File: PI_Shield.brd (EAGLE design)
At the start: 72.4 x 72.4 mm, 74 parts, among them J10 T2I, J11 T2I, J12 T2I, J13 DF13-4P-1.25DSA, J14 DF13-4P-1.25DSA, J15 DF13-4P-1.25DSA, J16 T2I5P, Q1 220mA/50V/3.5Ω, Q2 220mA/50V/3.5Ω, Q3 220mA/50V/3.5Ω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

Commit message: General routing complete
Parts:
- moved C3 4.40 mm to (33.4, 45.6), flipped to the top
- moved R8 1.66 mm to (45.3, 25.0), turned to 180 degrees
- moved J4 1.02 mm to (34.0, 58.9)
- moved R6 1.02 mm to (37.1, 63.1)
- moved C11 0.68 mm to (30.0, 34.3)
- moved R7 0.64 mm to (37.1, 65.2)
- moved J11 0.63 mm to (40.0, 58.2)
- moved J10 0.46 mm to (40.0, 65.8)
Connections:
- removed net 3VO: U$4.3VO, U$5.3VO
- removed net DI: U$8.31
- removed net DI3: U$8.40
- new net 3VO_1: U$4.3VO
- new net 3VO_2: U$5.3VO
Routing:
- net SDA: track 0.02 -> 123.6 mm, vias 0 -> 7
- net SCL: track 0.02 -> 119.0 mm, vias 0 -> 6
- net CAN_P: track 0.00 -> 45.7 mm, vias 0 -> 1
- net CAN_N: track 0.00 -> 45.3 mm, vias 0 -> 1
- net RXCAN: track 0.00 -> 16.0 mm, vias 0 -> 1
- net TXCAN: track 0.00 -> 15.8 mm, vias 0 -> 1
- net INT: track 0.00 -> 15.8 mm
- net CLK: track 14.8 -> 30.4 mm
- net MOSI: track 20.2 -> 33.7 mm
- net TX: track 0.00 -> 12.8 mm
- net RX0_INT: track 0.00 -> 12.7 mm
- net RX: track 0.00 -> 12.7 mm
- net MISO: track 18.3 -> 28.9 mm
- net DI2: track 0.00 -> 10.4 mm
- net DI1: track 0.00 -> 10.1 mm
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
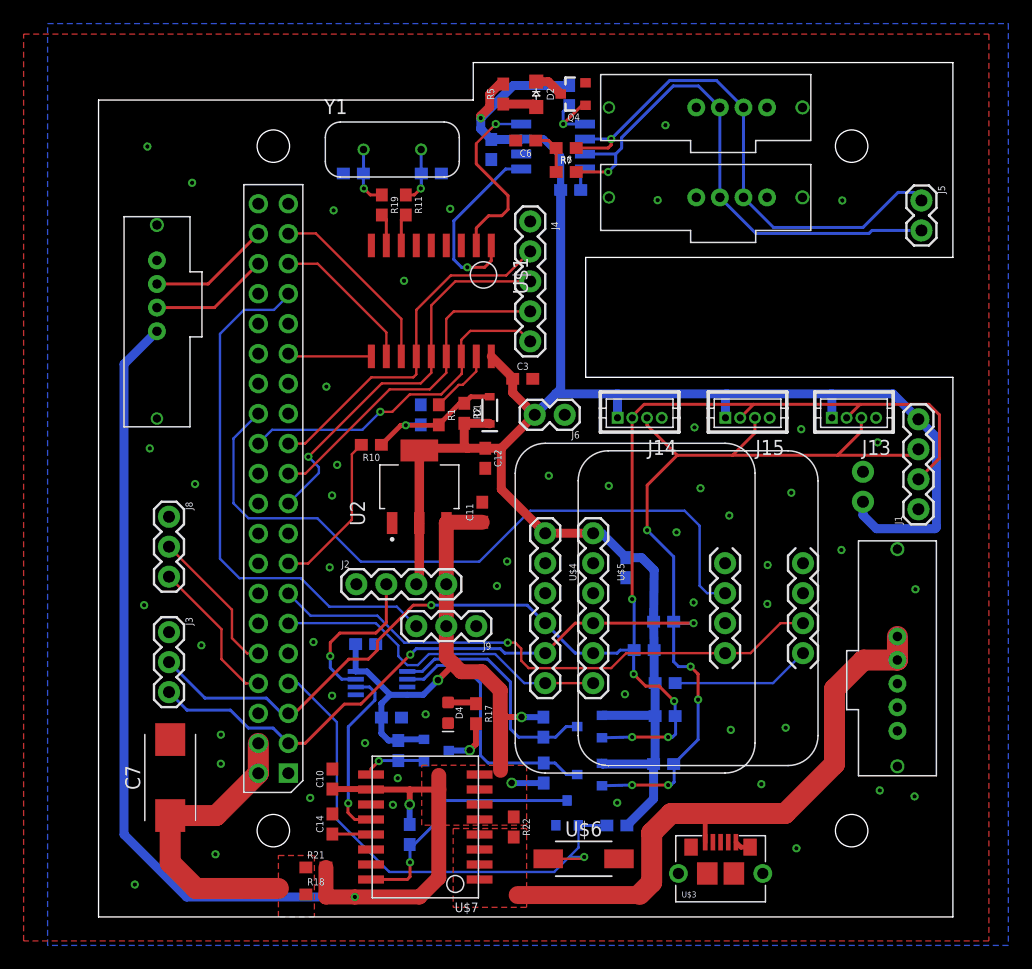
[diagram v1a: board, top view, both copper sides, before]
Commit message: Working on Impedance Matching
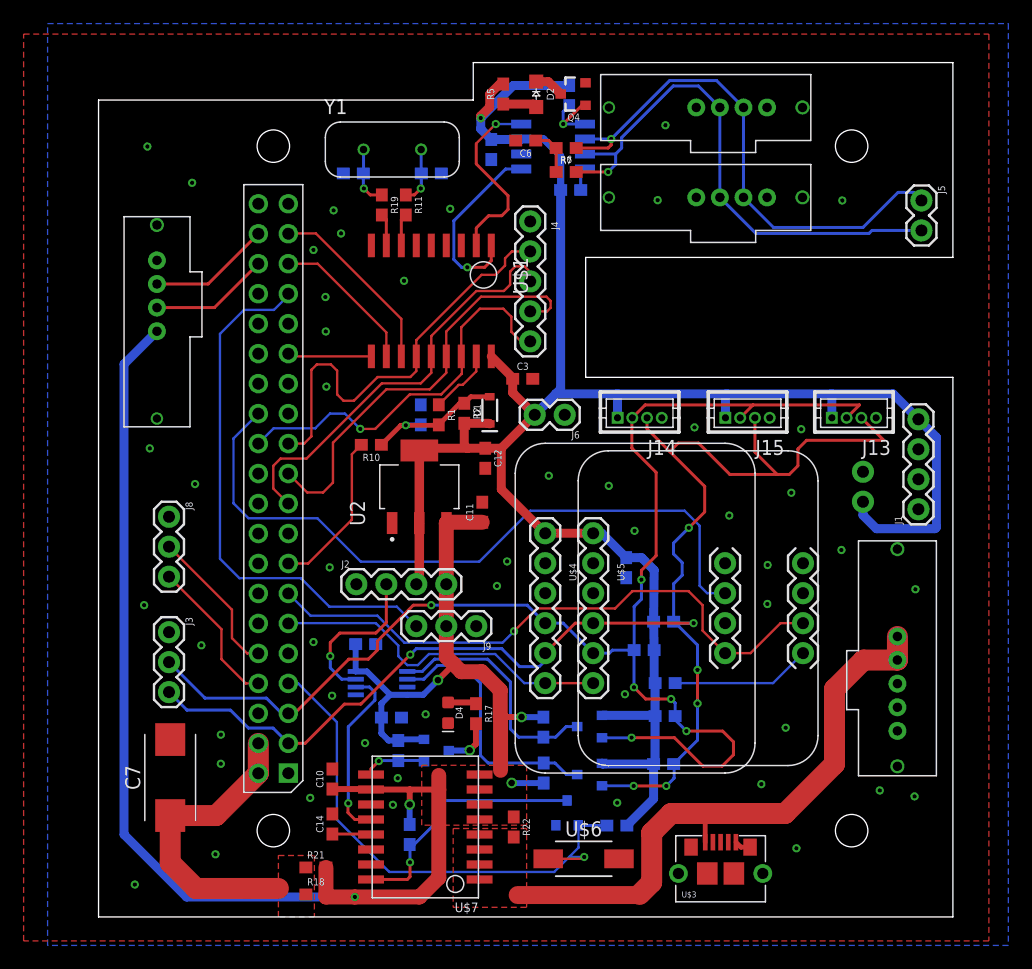
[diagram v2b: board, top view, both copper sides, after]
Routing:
- net MISO: track 28.9 -> 36.4 mm
- net CLK: track 30.4 -> 36.2 mm
- net CS: track 29.1 -> 33.1 mm
- net IMU_INT: track 48.4 -> 51.6 mm
- net SDA: track 123.6 -> 126.2 mm
- net MOSI: track 33.7 -> 36.0 mm, vias 1 -> 0
- net GND: vias 51 -> 49

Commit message: labels, routing touch ups, etc
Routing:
- net GND: track 1.37 -> 30.0 mm, vias 49 -> 65
- net SDA: track 126.2 -> 123.3 mm
- net SCL: track 119.4 -> 117.6 mm
- net 5V: track 152.5 -> 151.0 mm
- net OCD: track 9.96 -> 10.6 mm
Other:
- board size 72.4 x 72.4 mm -> 71.5 x 72.4 mm
- board text added: "5V - DI1 - DI2 - GND"
- board text added: "CAN_H - CAN_L"
- board text added: "CS - MISO - MOSI - CLK - GND"
- board text added: "GND - GND - NC - 5V - 5V"
- board text added: "GND - SCL - SDA - 3.3V"
- board text added: "PWM - 5V - GND"
- board text added: "SDA - SCL - GND"

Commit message: Finishing touches
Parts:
- added D3, D5: (no value), SparkFun-LED:LED-0603
- added R26, R27: (no value), SparkFun-Resistors:0603
- moved J12 7.79 mm to (6.25, 49.3)
- moved R17 3.18 mm to (26.3, 17.0), flipped to the bottom, turned to 180 degrees
- moved D4 2.65 mm to (29.5, 16.2)
- moved C8 1.86 mm to (20.4, 16.8), turned to 0 degrees
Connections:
- net CAN_N renamed CAN_L
- net CAN_P renamed CAN_H
- new net N$12: D5.A, R27.1
- new net N$9: D3.A, R26.1
- net 3V3: now also R27.2
- net 5V: now also R26.2
- net GND: now also D3.C, D5.C
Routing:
- net 3V3: track 183.8 -> 214.1 mm, vias 1 -> 2
- net SCL: track 117.6 -> 130.2 mm
- net 5V: track 151.0 -> 162.0 mm
- net SDA: track 123.3 -> 128.1 mm, vias 7 -> 8
- net GND: track 30.0 -> 33.9 mm, vias 65 -> 78
- net N$11: track 2.40 -> 6.29 mm, vias 0 -> 1
- net N$12: track 0.00 -> 3.85 mm
- net N$9: track 0.00 -> 3.06 mm, vias 0 -> 1
- net PI_POWER: track 25.6 -> 28.1 mm
- net SDA_ADC: track 22.3 -> 19.9 mm
- net DI2: track 10.4 -> 9.00 mm
- net N$10: track 4.25 -> 2.93 mm, vias 1 -> 0
- net DI1: track 10.1 -> 9.22 mm
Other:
- board size 71.5 x 72.4 mm -> 71.5 x 73 mm
- board text added: "3.3V - GND"
- board text added: "3.3V - SCL - SDA - GND"
- board text added: "3.3V LED"
- board text added: "5V LED"
- board text added: "<<<"
- board text added: "BNO055"
- board text added: "CAN FAULT LED"
- board text added: "FXOS8700 FXAS21002"
- board text added: "ODC LED"
- board text added: "TX - RX - GND"

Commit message: Added Image
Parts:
- moved D3 1.30 mm to (6.15, 45.7)
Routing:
- net N$9: track 3.06 -> 4.35 mm
- net GND: vias 78 -> 76
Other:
- board text added: "Overcurrent Fault"
- board text removed: "ODC LED"

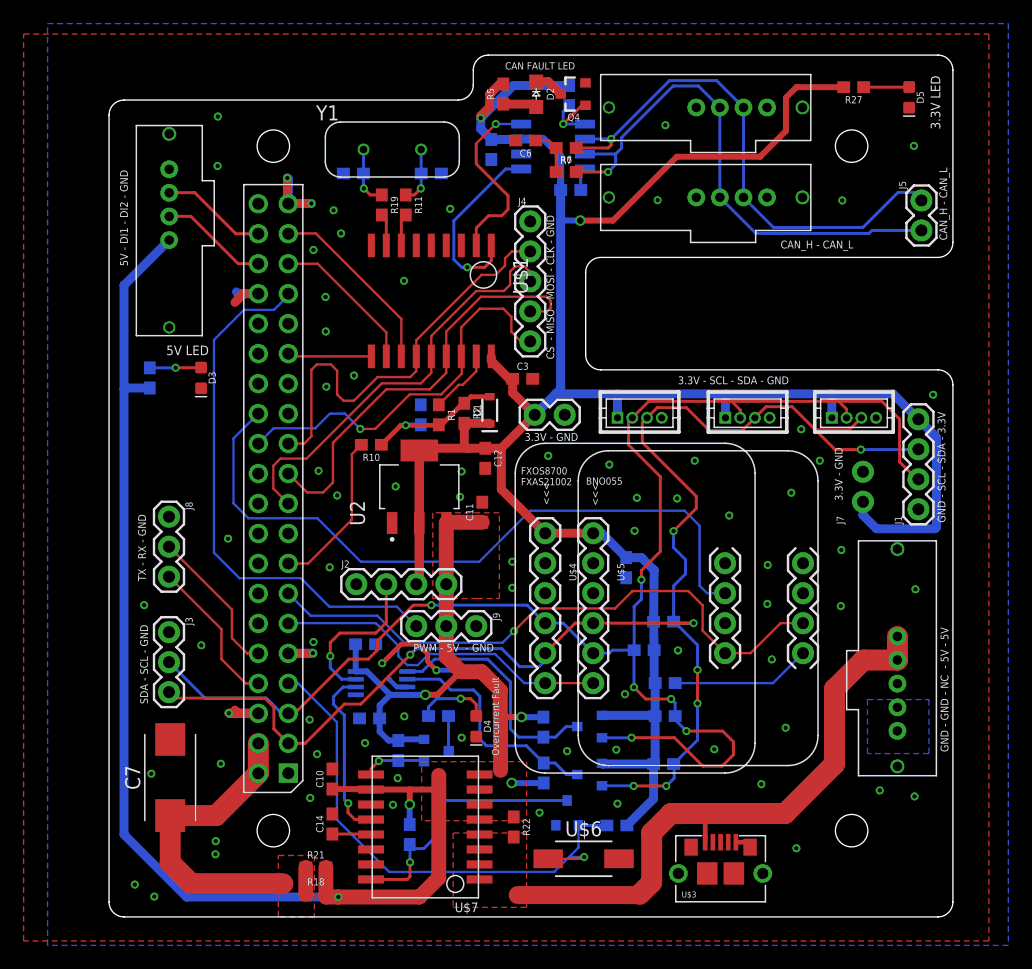
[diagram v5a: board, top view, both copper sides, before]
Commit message: Ordering text, step, and pdf
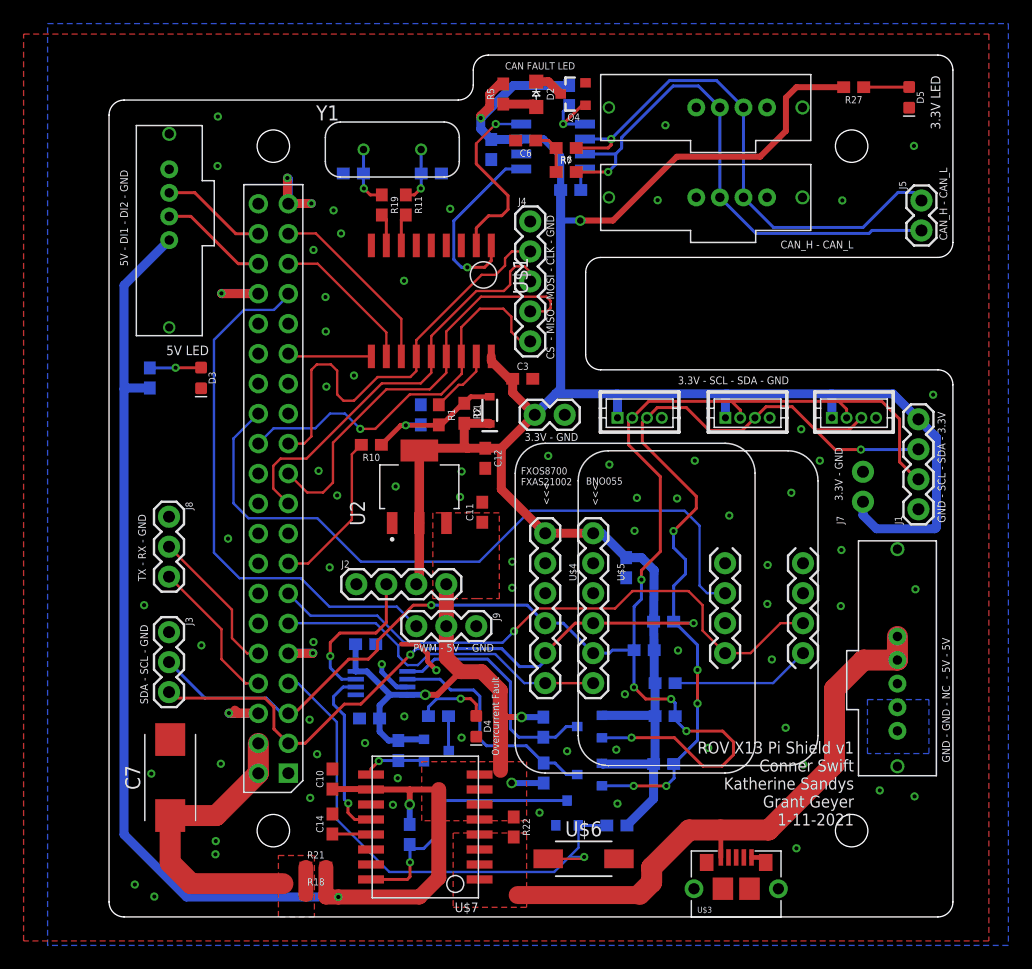
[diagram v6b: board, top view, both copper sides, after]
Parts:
- moved U$3 1.85 mm to (51.5, 2.39)
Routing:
- net 5V: track 162.0 -> 152.4 mm
- net 5V_RAW: track 51.1 -> 49.3 mm
- net GND: track 33.9 -> 33.2 mm, vias 76 -> 77
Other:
- board text added: "ROV X13 Pi Shield v1 Conner Swift Katherine Sandys Grant Geyer 1-11-2021"
